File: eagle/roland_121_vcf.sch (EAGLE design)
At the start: 100 parts, among them IC1 TL072P, IC2 LM13700N, IC3 LM13700N, Q1 2SK30, Q2 2N3904, Q3 2N3906, Q4 2SK30, Q5 2N3904, Q6 2SK30, Q8 2N3904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

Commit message: smt decouplers, shrouded power, 16 or 9mm pots
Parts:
- C3, C4, C5, C6, C7, C8: value 0.1uF -> 100n; device rcl:C-US025-030X050 -> rcl:C-USC1206
- renumbered C19 to C2
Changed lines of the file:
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@@
 <part name="P-14" library="supply1" deviceset="-12V" device=""/>
 <part name="P+14" library="supply1" deviceset="+12V" device=""/>
-<part name="C19" library="rcl" deviceset="CPOL-US" device="B45181A" value="10/25v BP"/>
 <part name="RESONANCE" library="pot" deviceset="3RP/1610N" device="" value="100k(A)"/>
 <part name="D1" library="diode" deviceset="1N4148" device="DO35-7"/>
@@
 <part name="CV2" library="solpad" deviceset="LSP10" device=""/>
 <part name="12DB_OUT" library="solpad" deviceset="LSP10" device=""/>
-<part name="C7" library="rcl" deviceset="C-US" device="025-030X050" value="0.1uF"/>
-<part name="C8" library="rcl" deviceset="C-US" device="025-030X050" value="0.1uF"/>
-<part name="C5" library="rcl" deviceset="C-US" device="025-030X050" value="0.1uF"/>
-<part name="C6" library="rcl" deviceset="C-US" device="025-030X050" value="0.1uF"/>
+<part name="C7" library="rcl" deviceset="C-US" device="C1206" value="100n"/>
+<part name="C8" library="rcl" deviceset="C-US" device="C1206" value="100n"/>
+<part name="C5" library="rcl" deviceset="C-US" device="C1206" value="100n"/>
+<part name="C6" library="rcl" deviceset="C-US" device="C1206" value="100n"/>
 <part name="GND11" library="supply1" deviceset="GND" device=""/>
 <part name="GND16" library="supply1" deviceset="GND" device=""/>
@@
 <part name="P+4" library="supply1" deviceset="+12V" device=""/>
 <part name="P-4" library="supply1" deviceset="-12V" device=""/>
-<part name="C3" library="rcl" deviceset="C-US" device="025-030X050" value="0.1uF"/>
-<part name="C4" library="rcl" deviceset="C-US" device="025-030X050" value="0.1uF"/>
+<part name="C3" library="rcl" deviceset="C-US" device="C1206" value="100n"/>
+<part name="C4" library="rcl" deviceset="C-US" device="C1206" value="100n"/>
 <part name="GND8" library="supply1" deviceset="GND" device=""/>
 <part name="FB1" library="adafruit" deviceset="FB" device=""/>
@@
 <part name="Q4" library="808" deviceset="2SK30" device=""/>
 <part name="Q6" library="808" deviceset="2SK30" device=""/>
+<part name="C2" library="rcl" deviceset="CPOL-US" device="B45181A" value="10/25v BP"/>
 </parts>
 <sheets>
@@
 <instance part="P-14" gate="1" x="292.1" y="15.24"/>
 <instance part="P+14" gate="1" x="292.1" y="58.42"/>
-<instance part="C19" gate="G$1" x="307.34" y="30.48" smashed="yes" rot="R90">
-<attribute name="NAME" x="306.705" y="31.496" size="1.778" layer="95" rot="R90"/>
-<attribute name="VALUE" x="311.531" y="31.496" size="1.778" layer="96" rot="R90"/>
-</instance>
 <instance part="RESONANCE" gate="G$1" x="149.86" y="-10.16" smashed="yes" rot="MR0">
 <attribute name="NAME" x="155.829" y="-13.97" size="1.778" layer="95" rot="MR90"/>
@@
 <attribute name="NAME" x="45.847" y="40.64" size="1.778" layer="95" rot="R90"/>
 <attribute name="VALUE" x="48.26" y="40.64" size="1.778" layer="96" rot="R90"/>
+</instance>
+<instance part="C2" gate="G$1" x="307.34" y="30.48" smashed="yes" rot="R90">
+<attribute name="NAME" x="306.705" y="31.496" size="1.778" layer="95" rot="R90"/>
+<attribute name="VALUE" x="311.531" y="31.496" size="1.778" layer="96" rot="R90"/>
 </instance>
 </instances>
@@
 <wire x1="314.96" y1="30.48" x2="312.42" y2="30.48" width="0.1524" layer="91"/>
 <pinref part="24DB_OUT" gate="1" pin="MP"/>
-<pinref part="C19" gate="G$1" pin="-"/>
+<pinref part="C2" gate="G$1" pin="-"/>
 </segment>
 </net>
@@
 <net name="N$36" class="0">
 <segment>
-<pinref part="C19" gate="G$1" pin="+"/>
-<pinref part="C19" gate="G$1" pin="+"/>
 <pinref part="Q8" gate="G1" pin="E"/>
 <pinref part="R58" gate="G$1" pin="2"/>
@@
 <wire x1="299.72" y1="10.16" x2="299.72" y2="30.48" width="0.1524" layer="91"/>
 <junction x="299.72" y="30.48"/>
+<junction x="299.72" y="30.48"/>
+<pinref part="C2" gate="G$1" pin="+"/>
 <wire x1="304.8" y1="30.48" x2="299.72" y2="30.48" width="0.1524" layer="91"/>
-<junction x="304.8" y="30.48"/>
 <junction x="299.72" y="30.48"/>
 </segment>

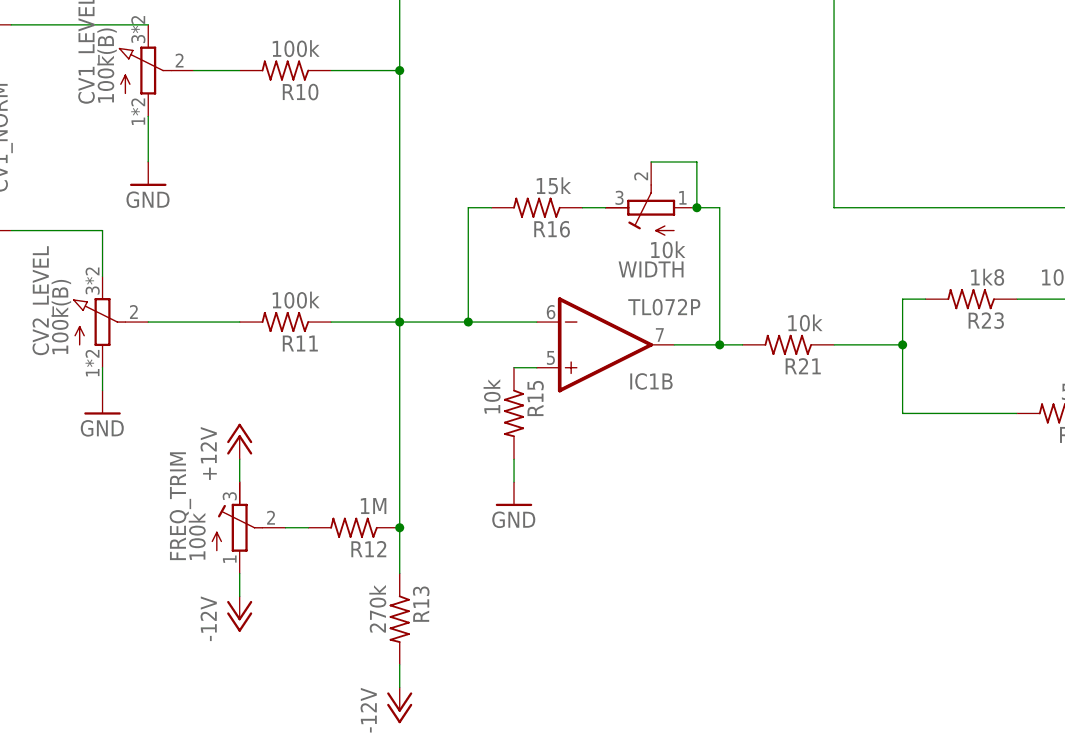
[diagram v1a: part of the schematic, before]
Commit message: now with flexible trimmer pinout
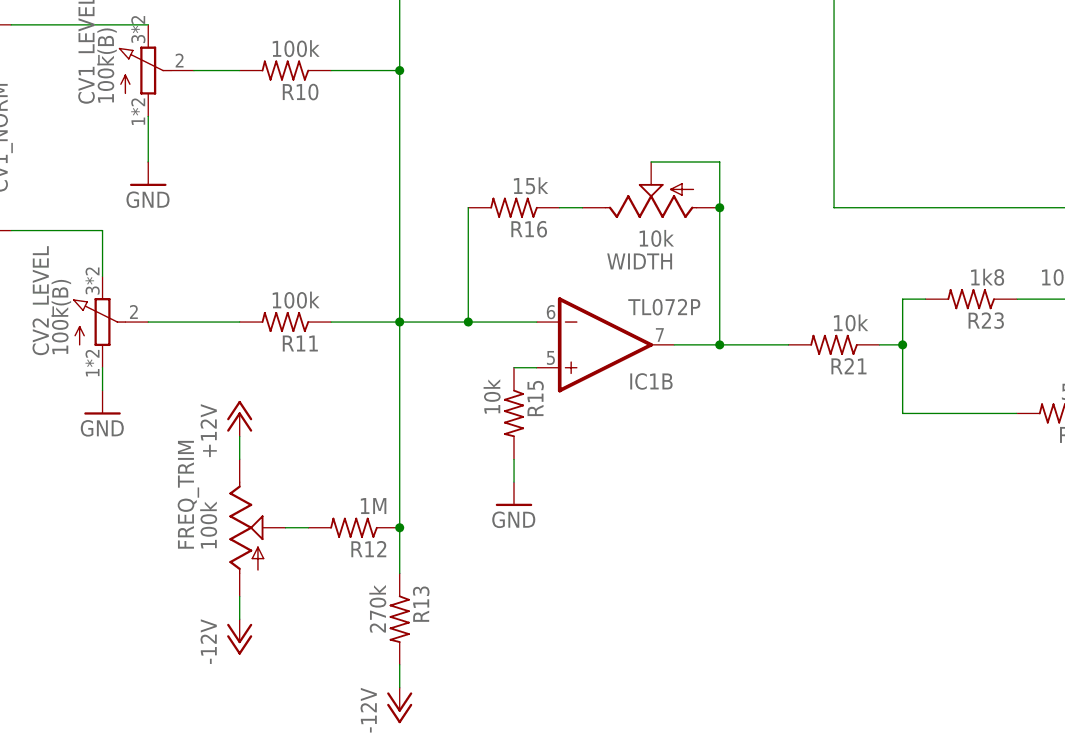
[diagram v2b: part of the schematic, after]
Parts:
- FREQ_TRIM, WIDTH: device rcl:R-TRIMM64W -> pot:TRIM_US-B64W
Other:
- moved on the sheet: R16, R21
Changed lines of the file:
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@@
 <part name="R16" library="rcl" deviceset="R-US_" device="0207/7" value="15k"/>
 <part name="R21" library="rcl" deviceset="R-US_" device="0207/7" value="10k"/>
-<part name="WIDTH" library="rcl" deviceset="R-TRIMM" device="64W" value="10k"/>
 <part name="R14" library="rcl" deviceset="R-US_" device="0207/7" value="33k"/>
 <part name="GND9" library="supply1" deviceset="GND" device=""/>
 <part name="GND10" library="supply1" deviceset="GND" device=""/>
 <part name="R13" library="rcl" deviceset="R-US_" device="0207/7" value="270k"/>
-<part name="FREQ_TRIM" library="rcl" deviceset="R-TRIMM" device="64W" value="100k"/>
 <part name="R12" library="rcl" deviceset="R-US_" device="0207/7" value="1M"/>
 <part name="R15" library="rcl" deviceset="R-US_" device="0207/7" value="10k"/>
@@
 <part name="Q6" library="808" deviceset="2SK30" device=""/>
 <part name="C2" library="rcl" deviceset="CPOL-US" device="B45181A" value="10/25v BP"/>
+<part name="FREQ_TRIM" library="pot" deviceset="TRIM_US-" device="B64W" value="100k"/>
+<part name="WIDTH" library="pot" deviceset="TRIM_US-" device="B64W" value="10k"/>
 </parts>
 <sheets>
@@
 <attribute name="VALUE" x="-13.97" y="61.722" size="1.778" layer="96" rot="R180"/>
 </instance>
-<instance part="R16" gate="G$1" x="-43.18" y="0" smashed="yes" rot="R180">
-<attribute name="NAME" x="-39.37" y="-1.4986" size="1.778" layer="95" rot="R180"/>
-<attribute name="VALUE" x="-39.37" y="3.302" size="1.778" layer="96" rot="R180"/>
-</instance>
-<instance part="R21" gate="G$1" x="-15.24" y="-15.24" smashed="yes" rot="R180">
-<attribute name="NAME" x="-11.43" y="-16.7386" size="1.778" layer="95" rot="R180"/>
-<attribute name="VALUE" x="-11.43" y="-11.938" size="1.778" layer="96" rot="R180"/>
-</instance>
-<instance part="WIDTH" gate="G$1" x="-30.48" y="0" smashed="yes" rot="R90">
-<attribute name="NAME" x="-26.67" y="-5.969" size="1.778" layer="95" rot="R180"/>
-<attribute name="VALUE" x="-26.67" y="-3.81" size="1.778" layer="96" rot="R180"/>
+<instance part="R16" gate="G$1" x="-45.72" y="0" smashed="yes" rot="R180">
+<attribute name="NAME" x="-41.91" y="-1.4986" size="1.778" layer="95" rot="R180"/>
+<attribute name="VALUE" x="-41.91" y="3.302" size="1.778" layer="96" rot="R180"/>
+</instance>
+<instance part="R21" gate="G$1" x="-10.16" y="-15.24" smashed="yes" rot="R180">
+<attribute name="NAME" x="-6.35" y="-16.7386" size="1.778" layer="95" rot="R180"/>
+<attribute name="VALUE" x="-6.35" y="-11.938" size="1.778" layer="96" rot="R180"/>
 </instance>
 <instance part="R14" gate="G$1" x="-53.34" y="50.8" smashed="yes" rot="R270">
@@
 <attribute name="VALUE" x="-61.722" y="-41.91" size="1.778" layer="96" rot="R270"/>
 </instance>
-<instance part="FREQ_TRIM" gate="G$1" x="-76.2" y="-35.56" smashed="yes">
-<attribute name="NAME" x="-82.169" y="-39.37" size="1.778" layer="95" rot="R90"/>
-<attribute name="VALUE" x="-80.01" y="-39.37" size="1.778" layer="96" rot="R90"/>
-</instance>
 <instance part="R12" gate="G$1" x="-63.5" y="-35.56" smashed="yes" rot="R180">
 <attribute name="NAME" x="-59.69" y="-37.0586" size="1.778" layer="95" rot="R180"/>
@@
 </instance>
 <instance part="P-3" gate="1" x="-58.42" y="-55.88"/>
-<instance part="P+3" gate="1" x="-76.2" y="-25.4"/>
-<instance part="P-2" gate="1" x="-76.2" y="-45.72"/>
+<instance part="P+3" gate="1" x="-76.2" y="-22.86"/>
+<instance part="P-2" gate="1" x="-76.2" y="-48.26"/>
 <instance part="R23" gate="G$1" x="5.08" y="-10.16" smashed="yes" rot="R180">
 <attribute name="NAME" x="8.89" y="-11.6586" size="1.778" layer="95" rot="R180"/>
@@
 <attribute name="VALUE" x="311.531" y="31.496" size="1.778" layer="96" rot="R90"/>
 </instance>
+<instance part="FREQ_TRIM" gate="G$1" x="-76.2" y="-35.56"/>
+<instance part="WIDTH" gate="G$1" x="-30.48" y="0" rot="R90"/>
 </instances>
 <busses>
@@
 <net name="+12V" class="0">
 <segment>
+<pinref part="P+3" gate="1" pin="+12V"/>
+<wire x1="-76.2" y1="-25.4" x2="-76.2" y2="-27.94" width="0.1524" layer="91"/>
 <pinref part="FREQ_TRIM" gate="G$1" pin="E"/>
-<pinref part="P+3" gate="1" pin="+12V"/>
-<wire x1="-76.2" y1="-27.94" x2="-76.2" y2="-30.48" width="0.1524" layer="91"/>
 </segment>
 <segment>
@@
 </segment>
 <segment>
+<pinref part="P-2" gate="1" pin="-12V"/>
+<wire x1="-76.2" y1="-45.72" x2="-76.2" y2="-43.18" width="0.1524" layer="91"/>
 <pinref part="FREQ_TRIM" gate="G$1" pin="A"/>
-<pinref part="P-2" gate="1" pin="-12V"/>
-<wire x1="-76.2" y1="-43.18" x2="-76.2" y2="-40.64" width="0.1524" layer="91"/>
 </segment>
 <segment>
@@
 <net name="N$9" class="0">
 <segment>
+<pinref part="R16" gate="G$1" pin="1"/>
+<wire x1="-40.64" y1="0" x2="-38.1" y2="0" width="0.1524" layer="91"/>
 <pinref part="WIDTH" gate="G$1" pin="E"/>
-<pinref part="R16" gate="G$1" pin="1"/>
-<wire x1="-38.1" y1="0" x2="-35.56" y2="0" width="0.1524" layer="91"/>
 </segment>
 </net>
@@
 <pinref part="R15" gate="G$1" pin="1"/>
 <wire x1="-45.72" y1="-17.78" x2="-43.18" y2="-17.78" width="0.1524" layer="91"/>
-</segment>
-</net>
-<net name="N$13" class="0">
-<segment>
-<pinref part="IC1" gate="B" pin="OUT"/>
-<pinref part="R21" gate="G$1" pin="2"/>
-<wire x1="-20.32" y1="-15.24" x2="-22.86" y2="-15.24" width="0.1524" layer="91"/>
-<wire x1="-22.86" y1="-15.24" x2="-27.94" y2="-15.24" width="0.1524" layer="91"/>
-<wire x1="-22.86" y1="-15.24" x2="-22.86" y2="0" width="0.1524" layer="91"/>
-<junction x="-22.86" y="-15.24"/>
-<pinref part="WIDTH" gate="G$1" pin="S"/>
-<pinref part="WIDTH" gate="G$1" pin="A"/>
-<wire x1="-30.48" y1="5.08" x2="-25.4" y2="5.08" width="0.1524" layer="91"/>
-<wire x1="-25.4" y1="5.08" x2="-25.4" y2="0" width="0.1524" layer="91"/>
-<wire x1="-22.86" y1="0" x2="-25.4" y2="0" width="0.1524" layer="91"/>
-<junction x="-25.4" y="0"/>
 </segment>
 </net>
@@
 <wire x1="-58.42" y1="-12.7" x2="-50.8" y2="-12.7" width="0.1524" layer="91"/>
 <wire x1="-50.8" y1="-12.7" x2="-43.18" y2="-12.7" width="0.1524" layer="91"/>
-<wire x1="-48.26" y1="0" x2="-50.8" y2="0" width="0.1524" layer="91"/>
 <wire x1="-50.8" y1="0" x2="-50.8" y2="-12.7" width="0.1524" layer="91"/>
 <junction x="-50.8" y="-12.7"/>
@@
 <net name="N$17" class="0">
 <segment>
-<pinref part="FREQ_TRIM" gate="G$1" pin="S"/>
 <pinref part="R12" gate="G$1" pin="2"/>
 <wire x1="-71.12" y1="-35.56" x2="-68.58" y2="-35.56" width="0.1524" layer="91"/>
+<pinref part="FREQ_TRIM" gate="G$1" pin="S"/>
 </segment>
 </net>
@@
 <pinref part="R21" gate="G$1" pin="1"/>
 <pinref part="R23" gate="G$1" pin="2"/>
-<wire x1="-10.16" y1="-15.24" x2="-2.54" y2="-15.24" width="0.1524" layer="91"/>
+<wire x1="-5.08" y1="-15.24" x2="-2.54" y2="-15.24" width="0.1524" layer="91"/>
 <wire x1="-2.54" y1="-15.24" x2="-2.54" y2="-10.16" width="0.1524" layer="91"/>
 <wire x1="-2.54" y1="-10.16" x2="0" y2="-10.16" width="0.1524" layer="91"/>
@@
 </segment>
 </net>
+<net name="N$38" class="0">
+<segment>
+<pinref part="WIDTH" gate="G$1" pin="S"/>
+<pinref part="WIDTH" gate="G$1" pin="A"/>
+<wire x1="-30.48" y1="5.08" x2="-22.86" y2="5.08" width="0.1524" layer="91"/>
+<wire x1="-22.86" y1="5.08" x2="-22.86" y2="0" width="0.1524" layer="91"/>
+<pinref part="IC1" gate="B" pin="OUT"/>
+<pinref part="R21" gate="G$1" pin="2"/>
+<wire x1="-15.24" y1="-15.24" x2="-22.86" y2="-15.24" width="0.1524" layer="91"/>
+<wire x1="-22.86" y1="-15.24" x2="-27.94" y2="-15.24" width="0.1524" layer="91"/>
+<wire x1="-22.86" y1="0" x2="-22.86" y2="-15.24" width="0.1524" layer="91"/>
+<junction x="-22.86" y="0"/>
+<junction x="-22.86" y="-15.24"/>
+</segment>
+</net>

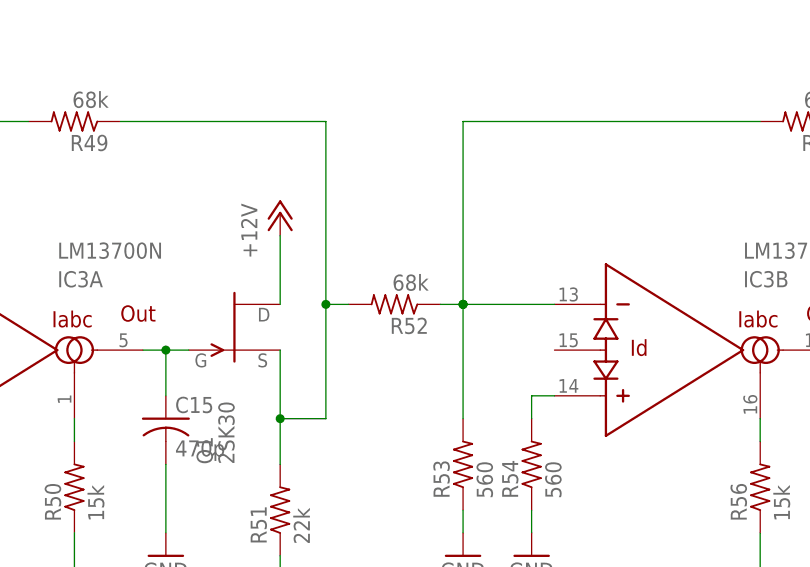
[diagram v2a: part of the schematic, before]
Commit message: fixed the wrong valued resistor
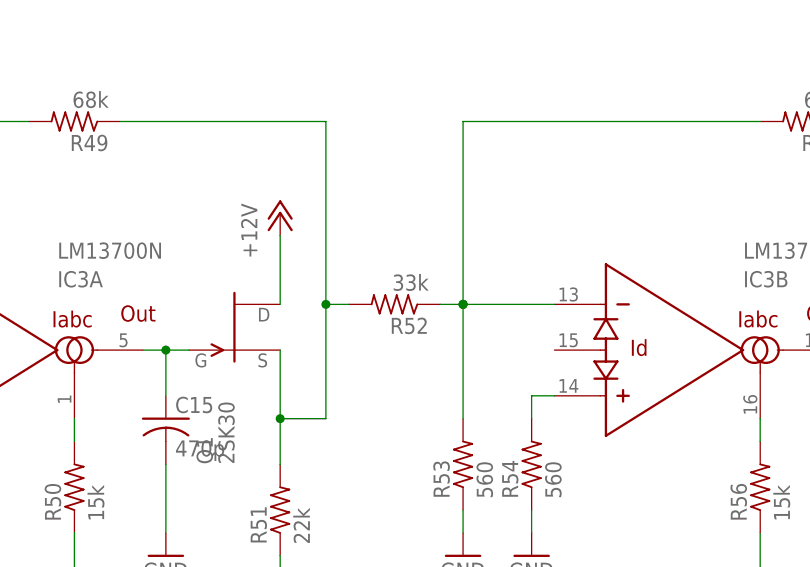
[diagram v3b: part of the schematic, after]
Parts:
- R52: value 68k -> 33k
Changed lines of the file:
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@@
 <part name="R31" library="rcl" deviceset="R-US_" device="0207/7" value="68k"/>
 <part name="R39" library="rcl" deviceset="R-US_" device="0207/7" value="68k"/>
-<part name="R52" library="rcl" deviceset="R-US_" device="0207/7" value="68k"/>
+<part name="R52" library="rcl" deviceset="R-US_" device="0207/7" value="33k"/>
 <part name="C11" library="rcl" deviceset="CPOL-US" device="B45181A" value="10/25v BP"/>
 <part name="Q5" library="transistor-npn" deviceset="2N3904" device=""/>
